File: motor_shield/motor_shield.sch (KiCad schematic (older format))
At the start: 23 parts, among them J2 Conn_01x04, J3 Conn_01x04, J4 Conn_01x04, J5 MOTOR PWR, J6 RPI PWR, J7 Raspberry_Pi_2_3, U1 DRV8834_CARRIER, U10 SHARP_GP2Y0A21YK0F, U2 DRV8834_CARRIER, U3 DRV8834_CARRIER, U4 ARDUINO_MICRO, U5 SHARP_GP2Y0A21YK0F, U6 SHARP_GP2Y0A21YK0F, U7 SHARP_GP2Y0A21YK0F, U8 SHARP_GP2Y0A21YK0F, U9 SHARP_GP2Y0A21YK0F

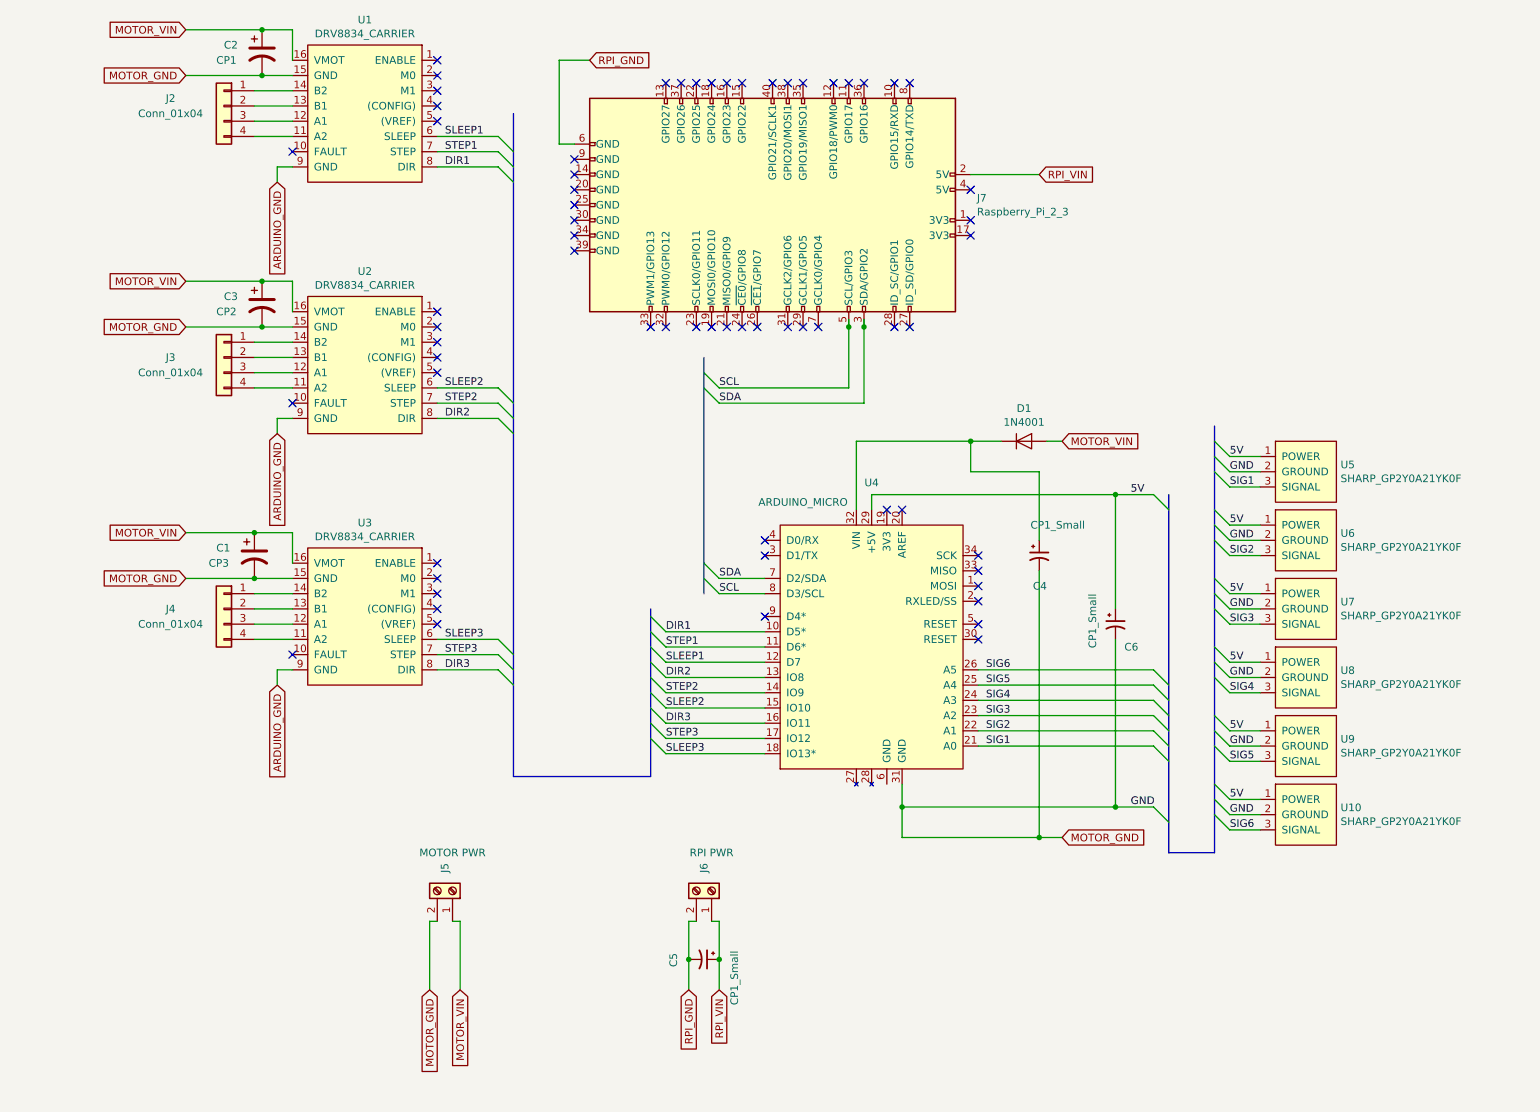
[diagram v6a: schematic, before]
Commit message: Remove the RPI connector and power supply
The board for holding the Arduino was too complicated, and
didn't allow me to use the protoshield on the RPI. This
also is 33% less expensive to fabricate.
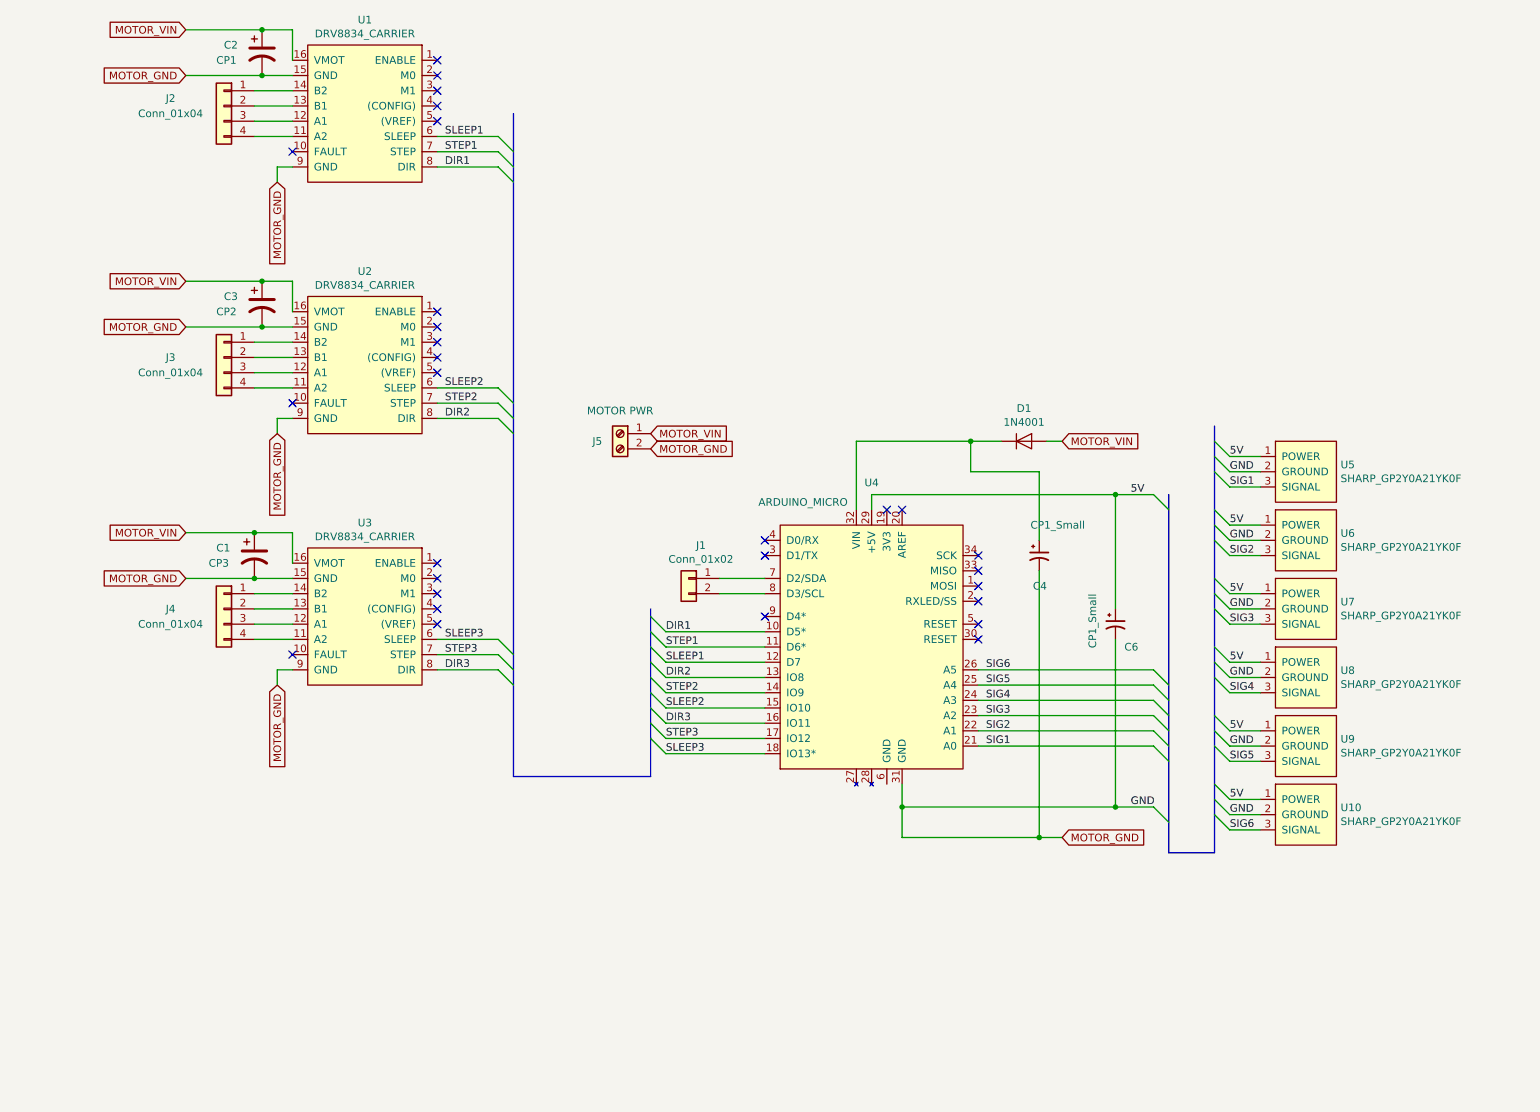
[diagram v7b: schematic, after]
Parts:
- removed C5: CP1_Small, Capacitor_THT:CP_Radial_D5.0mm_P2.50mm, symbol Device:CP1_Small
- removed J6: RPI PWR, CATPOO:TerminalBlock_Pololu-2_P5.00mm, symbol Connector:Screw_Terminal_01x02
- removed J7: Raspberry_Pi_2_3, Connector_PinHeader_2.54mm:PinHeader_2x20_P2.54mm_Vertical, symbol Connector:Raspberry_Pi_2_3
- added J1: Conn_01x02, Connector_JST:JST_XH_B02B-XH-A_1x02_P2.50mm_Vertical, symbol Connector_Generic:Conn_01x02
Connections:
- net ARDUINO_GND is gone; now on net MOTOR_GND: U1.9 (GND), U2.9 (GND), U3.9 (GND)
- net SCL: no longer names the net of U4.8 (D3/SCL)
- net SCL: now also J1.2 (Pin_2)
- net SDA: no longer names the net of U4.7 (D2/SDA)
- net SDA: now also J1.1 (Pin_1)
- no-connect marks 65 -> 29
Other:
- moved on the sheet: J5
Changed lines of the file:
@@
 	1850 2450 1350 2450
 Connection ~ 1850 2450
-Text GLabel 3150 7100 3    50   Input ~ 0
+Text GLabel 4400 3450 2    50   Input ~ 0
 MOTOR_VIN
-Text GLabel 2950 7100 3    50   Input ~ 0
+Text GLabel 4400 3550 2    50   Input ~ 0
 MOTOR_GND
-Text GLabel 4850 7100 3    50   Input ~ 0
-RPI_VIN
-Text GLabel 4650 7100 3    50   Input ~ 0
-RPI_GND
-Text GLabel 6950 1750 2    50   Input ~ 0
-RPI_VIN
-Text GLabel 4000 1000 2    50   Input ~ 0
-RPI_GND
 $Comp
 L CATPOO:SHARP_GP2Y0A21YK0F U7
@@
 L Connector:Screw_Terminal_01x02 J5
 U 1 1 5CDAA991
-P 3100 6450
-F 0 "J5" H 3250 6400 50  0000 C CNN
-F 1 "MOTOR PWR" V 3350 6450 50  0000 C CNN
-F 2 "CATPOO:TerminalBlock_Pololu-2_P5.00mm" H 3100 6450 50  0001 C CNN
-F 3 "~" H 3100 6450 50  0001 C CNN
-	1    3100 6450
-	0    1    -1   0
-$EndComp
-$Comp
-L Connector:Screw_Terminal_01x02 J6
-U 1 1 5CDB16D5
-P 4800 6450
-F 0 "J6" H 4950 6400 50  0000 C CNN
-F 1 "RPI PWR" V 5050 6450 50  0000 C CNN
-F 2 "CATPOO:TerminalBlock_Pololu-2_P5.00mm" H 4800 6450 50  0001 C CNN
-F 3 "~" H 4800 6450 50  0001 C CNN
-	1    4800 6450
-	0    1    -1   0
-$EndComp
-$Comp
-L Connector:Raspberry_Pi_2_3 J7
-U 1 1 5C82C37F
-P 5200 1950
-F 0 "J7" V 5154 3291 50  0000 L CNN
-F 1 "Raspberry_Pi_2_3" V 5245 3291 50  0000 L CNN
-F 2 "Connector_PinHeader_2.54mm:PinHeader_2x20_P2.54mm_Vertical" H 5200 1950 50  0001 C CNN
-F 3 "https://www.raspberrypi.org/documentation/hardware/raspberrypi/schematics/rpi_SCH_3bplus_1p0_reduced.pdf" H 5200 1950 50  0001 C CNN
-	1    5200 1950
-	0    1    1    0
-$EndComp
-Wire Wire Line
-	3000 6650 2950 6650
-Wire Wire Line
-	3150 6650 3100 6650
+P 4200 3450
+F 0 "J5" H 4350 3400 50  0000 C CNN
+F 1 "MOTOR PWR" H 4200 3600 50  0000 C CNN
+F 2 "CATPOO:TerminalBlock_Pololu-2_P5.00mm" H 4200 3450 50  0001 C CNN
+F 3 "~" H 4200 3450 50  0001 C CNN
+	1    4200 3450
+	-1   0    0    -1
+$EndComp
 Entry Wire Line
 	7700 5500 7800 5600
@@
 NoConn ~ 5950 3950
 NoConn ~ 6050 3950
-Text GLabel 1950 5100 3    50   Input ~ 0
-ARDUINO_GND
-Text GLabel 1950 3450 3    50   Input ~ 0
-ARDUINO_GND
-Text GLabel 1950 1800 3    50   Input ~ 0
-ARDUINO_GND
 Entry Wire Line
 	3400 1500 3500 1600
@@
 Text Label 4500 4950 0    50   ~ 0
 SLEEP1
-Wire Wire Line
-	5800 2700 5800 2750
-Wire Wire Line
-	5700 2700 5700 2750
-Wire Wire Line
-	6950 1750 6500 1750
-$Comp
-L Device:CP1_Small C5
-U 1 1 5C96E296
-P 4750 6900
-F 0 "C5" H 4800 6700 50  0000 R CNN
-F 1 "CP1_Small" H 5050 7100 50  0000 R CNN
-F 2 "Capacitor_THT:CP_Radial_D5.0mm_P2.50mm" H 4750 6900 50  0001 C CNN
-F 3 "~" H 4750 6900 50  0001 C CNN
-	1    4750 6900
-	0    1    1    0
-$EndComp
-Wire Wire Line
-	4650 6650 4700 6650
-Wire Wire Line
-	4800 6650 4850 6650
-Wire Wire Line
-	4000 1000 3800 1000
-Wire Wire Line
-	3800 1000 3800 1550
-Wire Wire Line
-	3800 1550 3900 1550
-NoConn ~ 6100 1150
-NoConn ~ 6000 1150
-NoConn ~ 5800 1150
-NoConn ~ 5700 1150
-NoConn ~ 5600 1150
-NoConn ~ 5400 1150
-NoConn ~ 5300 1150
-NoConn ~ 5200 1150
-NoConn ~ 5000 1150
-NoConn ~ 4900 1150
-NoConn ~ 4800 1150
-NoConn ~ 4700 1150
-NoConn ~ 4600 1150
-NoConn ~ 4500 1150
-NoConn ~ 3900 2250
-NoConn ~ 3900 2150
-NoConn ~ 3900 2050
-NoConn ~ 3900 1950
-NoConn ~ 3900 1850
-NoConn ~ 3900 1750
-NoConn ~ 3900 1650
-NoConn ~ 4400 2750
-NoConn ~ 4500 2750
-NoConn ~ 4700 2750
-NoConn ~ 4800 2750
-NoConn ~ 4900 2750
-NoConn ~ 5000 2750
-NoConn ~ 5100 2750
-NoConn ~ 5300 2750
-NoConn ~ 5400 2750
-NoConn ~ 5500 2750
-NoConn ~ 6000 2750
-NoConn ~ 6100 2750
-NoConn ~ 6500 2150
-NoConn ~ 6500 2050
-NoConn ~ 6500 1850
 NoConn ~ 5150 4250
 NoConn ~ 5150 4150
@@
 Wire Wire Line
 	7450 4800 7450 5900
-Wire Wire Line
-	4850 6650 4850 6900
-Wire Wire Line
-	4650 6650 4650 6900
-Connection ~ 4850 6900
-Wire Wire Line
-	4850 6900 4850 7100
-Connection ~ 4650 6900
-Wire Wire Line
-	4650 6900 4650 7100
 $Comp
 L CATPOO:ARDUINO_MICRO U4
@@
 Wire Wire Line
 	7000 3500 7100 3500
-Entry Wire Line
-	4750 4300 4850 4400
-Entry Wire Line
-	4750 4400 4850 4500
-Wire Wire Line
-	5150 4400 4850 4400
-Wire Wire Line
-	4850 4500 5150 4500
-Entry Wire Line
-	4750 3050 4850 3150
-Entry Wire Line
-	4750 3150 4850 3250
-Wire Wire Line
-	5800 2750 5800 3250
-Wire Wire Line
-	5800 3250 4850 3250
-Connection ~ 5800 2750
-Wire Wire Line
-	4850 3150 5700 3150
-Wire Wire Line
-	5700 3150 5700 2750
-Connection ~ 5700 2750
-Text Label 4850 3150 0    50   ~ 0
-SCL
-Text Label 4850 4500 0    50   ~ 0
-SCL
-Text Label 4850 4400 0    50   ~ 0
-SDA
-Text Label 4850 3250 0    50   ~ 0
-SDA
-Wire Wire Line
-	3150 6650 3150 7100
-Wire Wire Line
-	2950 6650 2950 7100
 Wire Wire Line
 	6950 4150 6950 3700
@@
 	6050 6100 6050 5900
 Connection ~ 6050 5900
-Wire Bus Line
-	4750 2950 4750 4500
+Wire Wire Line
+	4850 4400 5150 4400
+Wire Wire Line
+	5150 4500 4850 4500
+$Comp
+L Connector_Generic:Conn_01x02 J1
+U 1 1 5C9F7062
+P 4650 4400
+F 0 "J1" H 4570 4617 50  0000 C CNN
+F 1 "Conn_01x02" H 4570 4526 50  0000 C CNN
+F 2 "Connector_JST:JST_XH_B02B-XH-A_1x02_P2.50mm_Vertical" H 4650 4400 50  0001 C CNN
+F 3 "~" H 4650 4400 50  0001 C CNN
+	1    4650 4400
+	-1   0    0    -1
+$EndComp
 Wire Bus Line
 	3500 1350 3500 5700
@@
 Wire Bus Line
 	8100 3400 8100 6200
+Text GLabel 1950 5100 3    50   Input ~ 0
+MOTOR_GND
+Text GLabel 1950 3450 3    50   Input ~ 0
+MOTOR_GND
+Text GLabel 1950 1800 3    50   Input ~ 0
+MOTOR_GND
 $EndSCHEMATC
